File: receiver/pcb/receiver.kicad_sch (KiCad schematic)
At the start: 23 parts, among them IC1 DRV8251DDAR, IC2 DRV8251DDAR

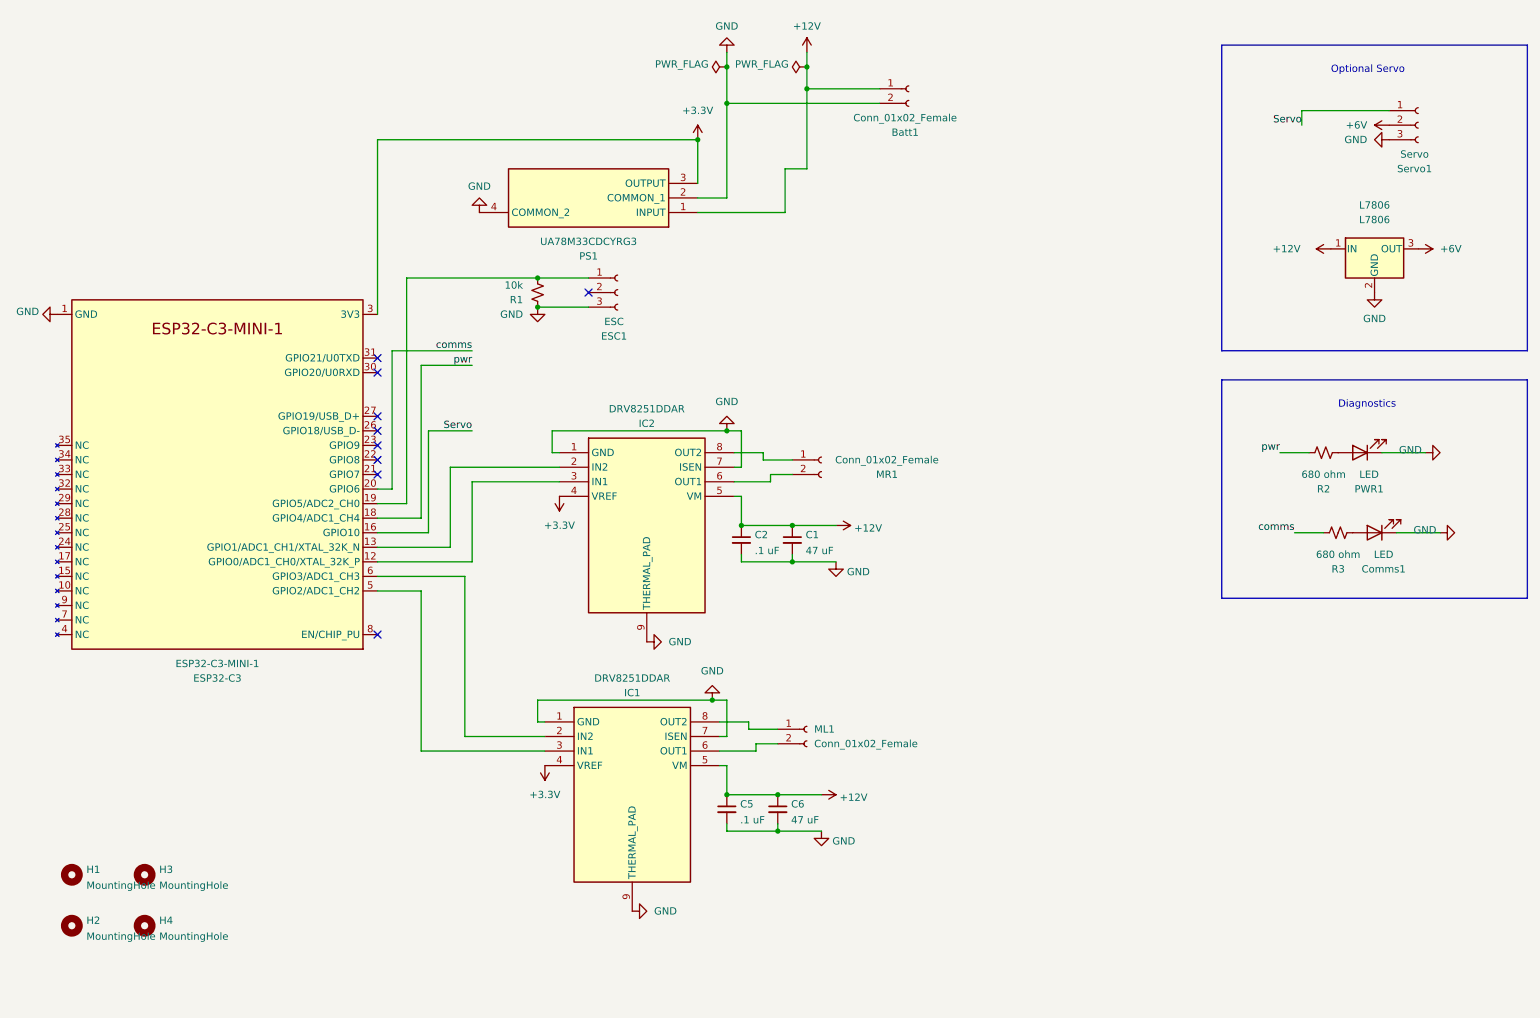
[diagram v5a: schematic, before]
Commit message: Receiver V5 as ordered.
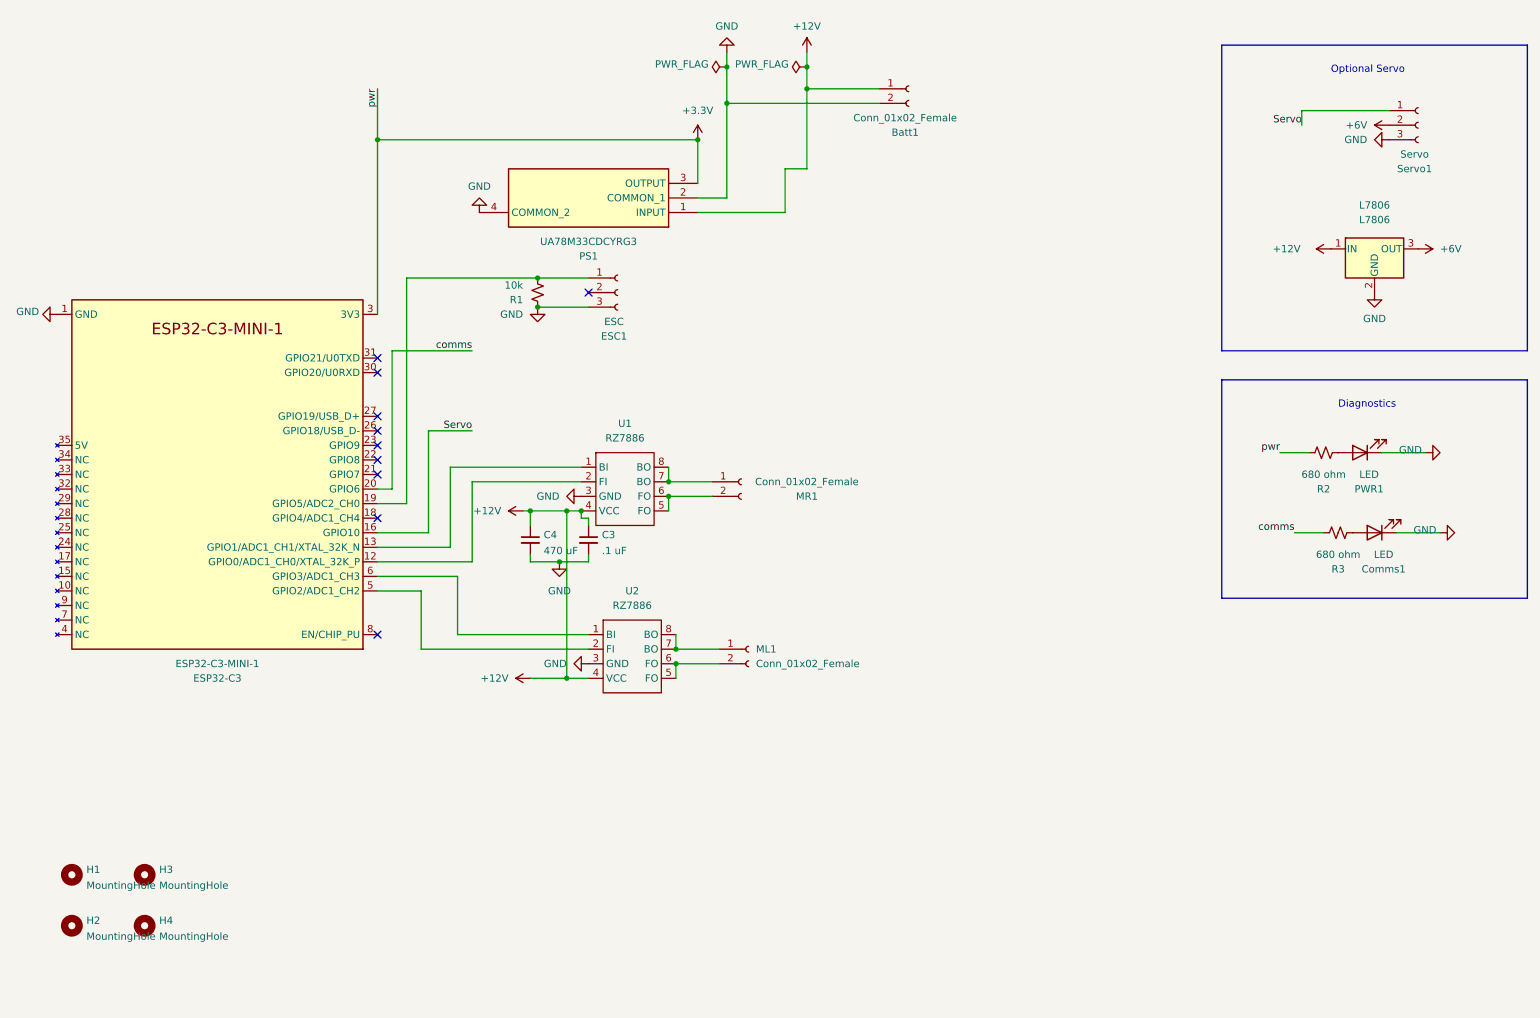
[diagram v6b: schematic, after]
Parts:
- removed C1, C6: 47 uF, Capacitor_SMD:C_0805_2012Metric_Pad1.18x1.45mm_HandSolder, symbol Device:C_Small
- removed C2, C5: .1 uF, Capacitor_SMD:C_0805_2012Metric_Pad1.18x1.45mm_HandSolder, symbol Device:C_Small
- removed IC1, IC2: DRV8251DDAR, drv8251:SOIC127P600X170-9N, symbol DRV8251:DRV8251DDAR
- added C3: .1 uF, Capacitor_SMD:C_0805_2012Metric_Pad1.18x1.45mm_HandSolder, symbol Device:C_Small
- added C4: 470 uF, Capacitor_THT:CP_Radial_D8.0mm_P3.80mm, symbol Device:C_Small
- added U1, U2: RZ7886, Package_DIP:DIP-8_W7.62mm, symbol RZ7886:RZ7886
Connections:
- net +12V: now also C3.1, C4.1, U1.4 (VCC), U2.4 (VCC)
- net +3V3: now also R2.1
- net GND: now also C3.2, C4.2, U1.3 (GND), U2.3 (GND)
- net at ML1.1 (Pin_1): now also U2.7 (BO), U2.8 (BO)
- net at ML1.2 (Pin_2): now also U2.5 (FO), U2.6 (FO)
- net at ESP32-C3.6 (GPIO3/ADC1_CH3): now also U2.1 (BI)
- net at ESP32-C3.5 (GPIO2/ADC1_CH2): now also U2.2 (FI)
- net at ESP32-C3.13 (GPIO1/ADC1_CH1/XTAL_32K_N): now also U1.1 (BI)
- net at ESP32-C3.12 (GPIO0/ADC1_CH0/XTAL_32K_P): now also U1.2 (FI)
- net at MR1.2 (Pin_2): now also U1.5 (FO), U1.6 (FO)
- net at MR1.1 (Pin_1): now also U1.7 (BO), U1.8 (BO)
- net pwr: no longer names the net of ESP32-C3.18 (GPIO4/ADC1_CH4)
- net pwr: no longer R2.1
- no-connect marks 9 -> 10
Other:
- moved on the sheet: ML1, MR1

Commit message: V6 receiver board as ordered. Rearranged things, improved symbols and footprints, bigger power traces, corrected L7806 footprint, additional diagnostic LED
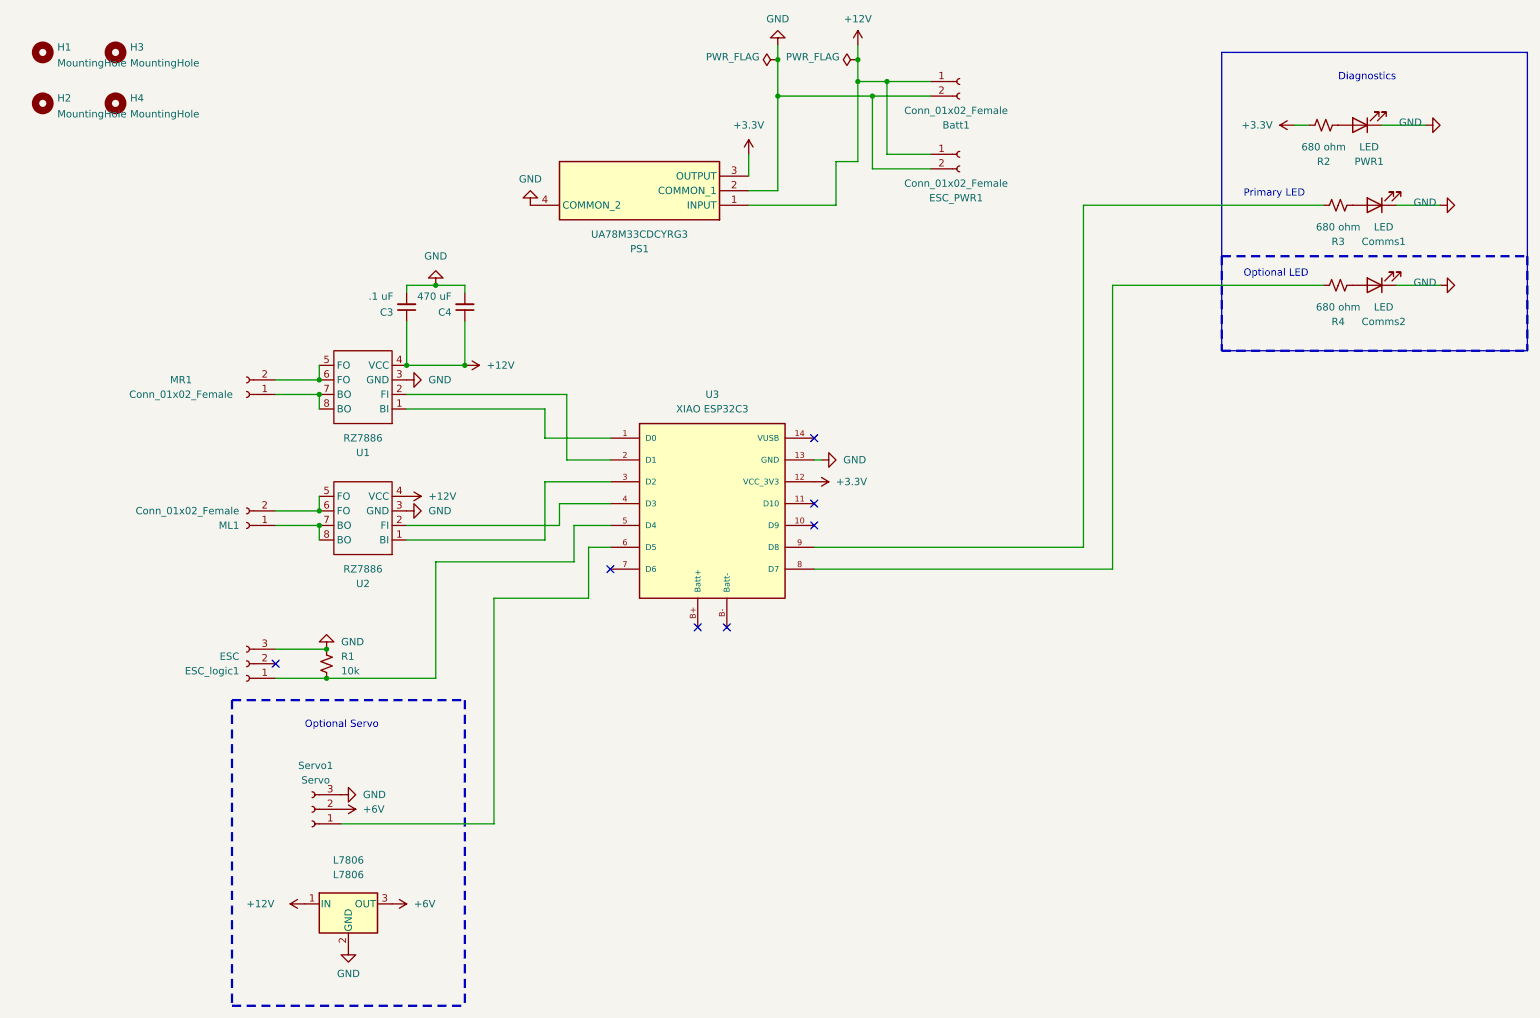
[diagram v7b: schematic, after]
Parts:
- removed ESP32-C3: ESP32-C3-MINI-1, Espressif:ESP32-C3, symbol Espressif:ESP32-C3-MINI-1
- added Comms2: LED, LED_SMD:LED_0805_2012Metric_Pad1.15x1.40mm_HandSolder, symbol Device:LED
- added ESC_PWR1: Conn_01x02_Female, custom:battery_pads, symbol Connector:Conn_01x02_Female
- added R4: 680 ohm, Resistor_SMD:R_0805_2012Metric_Pad1.20x1.40mm_HandSolder, symbol Device:R_Small_US
- added U3: XIAO ESP32C3, XIAO_ESP32C3:xiao_esp32c3, symbol xiao_esp32c3:XIAO ESP32C3
- Batt1: footprint battery:battery_pads -> custom:battery_pads
- L7806: footprint Package_TO_SOT_SMD:TO-252-3_TabPin2 -> Package_TO_SOT_SMD:TO-263-2_TabPin1
- renumbered ESC1 to ESC_logic1
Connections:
- net +12V: now also ESC_PWR1.1 (Pin_1)
- net +3V3: now also U3.12 (VCC_3V3)
- net GND: now also Comms2.1 (K), ESC_PWR1.2 (Pin_2), U3.13 (GND)
- net at ESC_logic1.1 (Pin_1), R1.2: now also U3.5 (D4)
- net at U1.2 (FI): now also U3.2 (D1)
- net at U1.1 (BI): now also U3.1 (D0)
- net at U2.2 (FI): now also U3.4 (D3)
- net at U2.1 (BI): now also U3.3 (D2)
- net Servo: no longer names the net of Servo1.1 (Pin_1)
- net Servo: now also U3.6 (D5)
- net comms: no longer names the net of R3.1
- net comms: now also U3.9 (D8)
- new net: R4.1, U3.8 (D7)
- new net: Comms2.2 (A), R4.2
- no-connect marks 10 -> 7
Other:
- note added: "Optional LED"
- note added: "Primary LED"
- moved on the sheet: Batt1, C3, C4, Comms1, ESC_logic1, H1, H2, H3, H4, L7806, ML1, MR1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

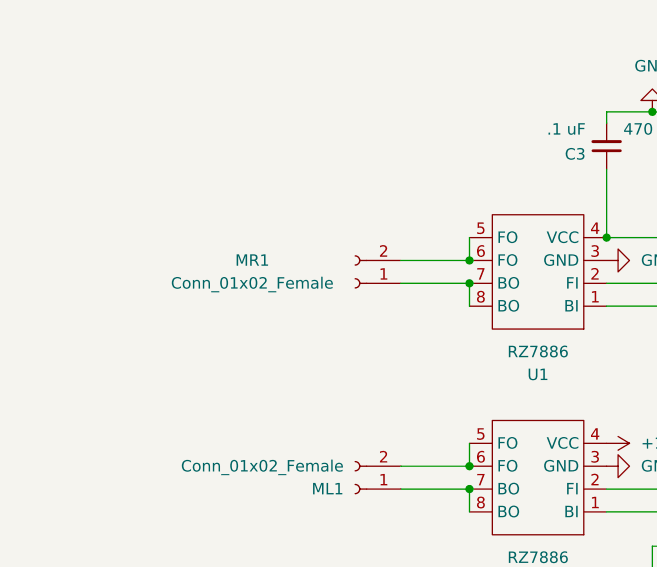
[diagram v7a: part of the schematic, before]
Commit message: fixed mistakenly small motor pads in receiver V6.
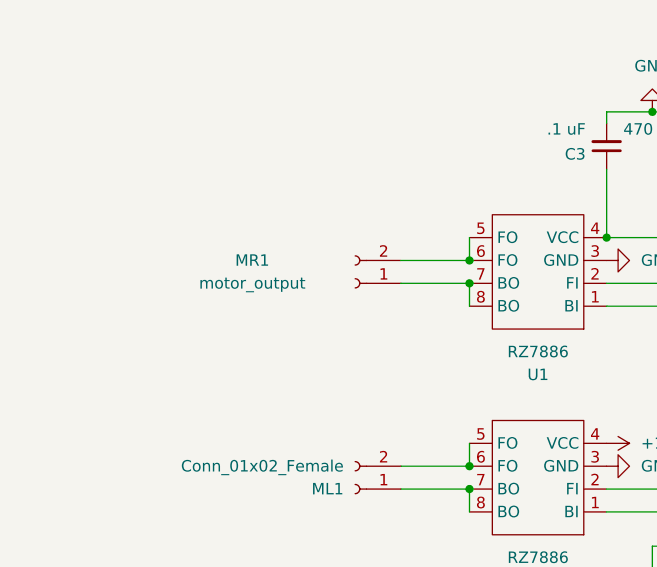
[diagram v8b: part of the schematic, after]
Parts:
- MR1: value Conn_01x02_Female -> motor_output; footprint Connector_PinSocket_2.54mm:PinSocket_1x02_P2.54mm_Vertical -> custom:DC_motor_output
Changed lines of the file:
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@@
       (effects (font (size 1.27 1.27)))
     )
-    (property "Value" "Conn_01x02_Female" (at 46.99 82.55 0)
+    (property "Value" "motor_output" (at 46.99 82.55 0)
       (effects (font (size 1.27 1.27)))
     )
-    (property "Footprint" "Connector_PinSocket_2.54mm:PinSocket_1x02_P2.54mm_Vertical" (at 58.42 82.55 0)
+    (property "Footprint" "custom:DC_motor_output" (at 58.42 82.55 0)
       (effects (font (size 1.27 1.27)) hide)
     )
